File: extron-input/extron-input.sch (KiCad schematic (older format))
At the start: 16 parts, among them J1 SCART-F, J10 Conn_01x01, J11 Conn_01x01, J2 Conn_Coaxial, J3 Conn_Coaxial, J4 Conn_Coaxial, J5 Conn_Coaxial, J6 Conn_01x03_Male, J7 Conn_01x02_Male, J8 Conn_01x01, J9 Conn_01x01, SW1 SW_DPDT_x2, U1 LM1881

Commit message: Oops, scart-input -> extron-input
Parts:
- J1: footprint scart-input:SCART_F_RA -> extron-input:SCART_F_RA
- J2, J3, J4, J5: footprint scart-input:BNC_90 -> extron-input:BNC_90
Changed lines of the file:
@@
 LIBS:power
 LIBS:74xx
-LIBS:scart-input-cache
+LIBS:extron-input-cache
 EELAYER 26 0
 EELAYER END
@@
 F 0 "J2" H 8200 1550 50  0000 L CNN
 F 1 "Conn_Coaxial" H 7850 2200 50  0000 L CNN
-F 2 "scart-input:BNC_90" H 8250 2050 50  0001 C CNN
+F 2 "extron-input:BNC_90" H 8250 2050 50  0001 C CNN
 F 3 " ~" H 8250 2050 50  0001 C CNN
 	1    8250 2050
@@
 F 0 "J3" H 8200 2400 50  0000 L CNN
 F 1 "Conn_Coaxial" H 7850 3050 50  0000 L CNN
-F 2 "scart-input:BNC_90" H 8250 2900 50  0001 C CNN
+F 2 "extron-input:BNC_90" H 8250 2900 50  0001 C CNN
 F 3 " ~" H 8250 2900 50  0001 C CNN
 	1    8250 2900
@@
 F 0 "J4" H 8200 3250 50  0000 L CNN
 F 1 "Conn_Coaxial" H 7850 3900 50  0000 L CNN
-F 2 "scart-input:BNC_90" H 8250 3750 50  0001 C CNN
+F 2 "extron-input:BNC_90" H 8250 3750 50  0001 C CNN
 F 3 " ~" H 8250 3750 50  0001 C CNN
 	1    8250 3750
@@
 F 0 "J5" H 8200 4050 50  0000 L CNN
 F 1 "Conn_Coaxial" H 7850 4700 50  0000 L CNN
-F 2 "scart-input:BNC_90" H 8250 4550 50  0001 C CNN
+F 2 "extron-input:BNC_90" H 8250 4550 50  0001 C CNN
 F 3 " ~" H 8250 4550 50  0001 C CNN
 	1    8250 4550
@@
 F 0 "J1" H 3850 4520 50  0000 C CNN
 F 1 "SCART-F" H 3850 4429 50  0000 C CNN
-F 2 "scart-input:SCART_F_RA" H 3850 3150 50  0001 C CNN
+F 2 "extron-input:SCART_F_RA" H 3850 3150 50  0001 C CNN
 F 3 " ~" H 3850 3150 50  0001 C CNN
 	1    3850 3100

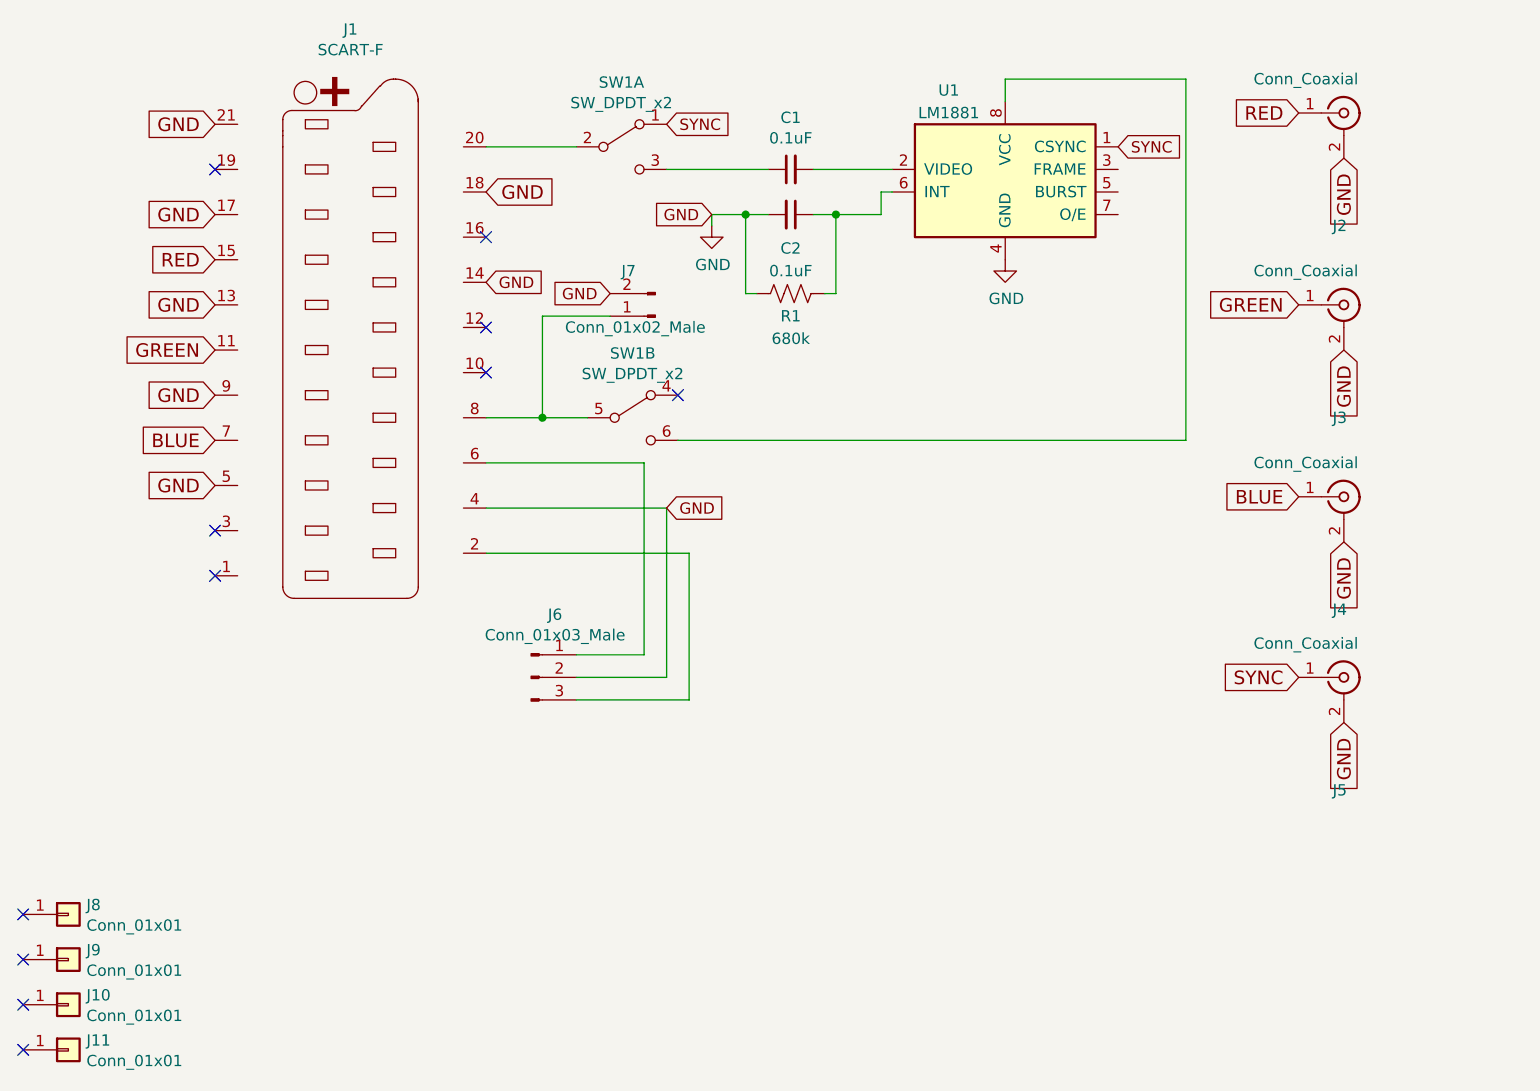
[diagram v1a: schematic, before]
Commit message: Random fixes to extron-input layout/schematic
There were some weirdnesses between the schematic and layout. I believe
these are fixed now.

I also switched the footprint to JST XH side connectors for both sense
and phoenix ports. I found that there are cables that can be purchased
for cheap for this form factor.
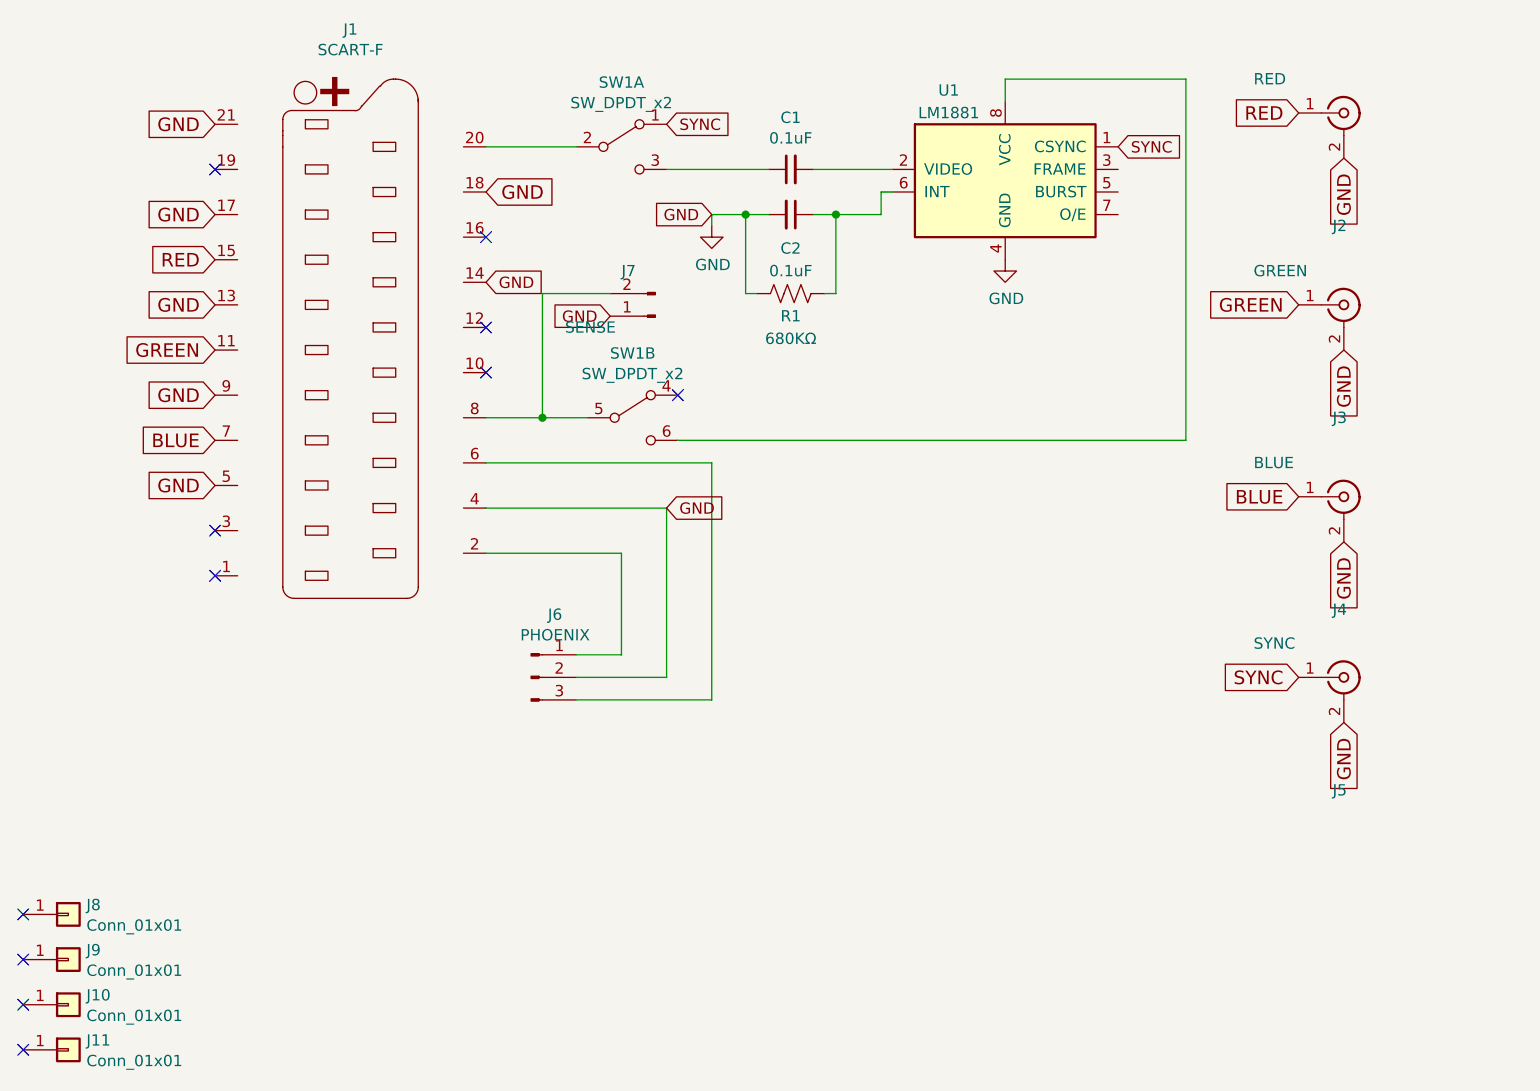
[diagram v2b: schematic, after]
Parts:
- J2: value Conn_Coaxial -> RED
- J3: value Conn_Coaxial -> GREEN
- J4: value Conn_Coaxial -> BLUE
- J5: value Conn_Coaxial -> SYNC
- J6: value Conn_01x03_Male -> PHOENIX; footprint Connector_JST:JST_EH_S03B-EH_1x03_P2.50mm_Horizontal -> Connector_JST:JST_XH_S03B-XH-A_1x03_P2.50mm_Horizontal
- J7: value Conn_01x02_Male -> SENSE; footprint Connector_JST:JST_EH_S02B-EH_1x02_P2.50mm_Horizontal -> Connector_JST:JST_XH_S02B-XH-A_1x02_P2.50mm_Horizontal
- R1: value 680k -> 680KΩ
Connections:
- net GND: now also J7.1 (Pin_1); no longer J7.2 (Pin_2)
- net at J1.2 (P2): now also J6.1 (Pin_1); no longer J6.3 (Pin_3)
- net at J1.6 (P6): now also J6.3 (Pin_3); no longer J6.1 (Pin_1)
- net at J1.8 (P8), SW1.5 (B): now also J7.2 (Pin_2); no longer J7.1 (Pin_1)
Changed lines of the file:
@@
 P 8250 2050
 F 0 "J2" H 8200 1550 50  0000 L CNN
-F 1 "Conn_Coaxial" H 7850 2200 50  0000 L CNN
+F 1 "RED" H 7850 2200 50  0000 L CNN
 F 2 "extron-input:BNC_90" H 8250 2050 50  0001 C CNN
 F 3 " ~" H 8250 2050 50  0001 C CNN
@@
 P 8250 2900
 F 0 "J3" H 8200 2400 50  0000 L CNN
-F 1 "Conn_Coaxial" H 7850 3050 50  0000 L CNN
+F 1 "GREEN" H 7850 3050 50  0000 L CNN
 F 2 "extron-input:BNC_90" H 8250 2900 50  0001 C CNN
 F 3 " ~" H 8250 2900 50  0001 C CNN
@@
 P 8250 3750
 F 0 "J4" H 8200 3250 50  0000 L CNN
-F 1 "Conn_Coaxial" H 7850 3900 50  0000 L CNN
+F 1 "BLUE" H 7850 3900 50  0000 L CNN
 F 2 "extron-input:BNC_90" H 8250 3750 50  0001 C CNN
 F 3 " ~" H 8250 3750 50  0001 C CNN
@@
 P 8250 4550
 F 0 "J5" H 8200 4050 50  0000 L CNN
-F 1 "Conn_Coaxial" H 7850 4700 50  0000 L CNN
+F 1 "SYNC" H 7850 4700 50  0000 L CNN
 F 2 "extron-input:BNC_90" H 8250 4550 50  0001 C CNN
 F 3 " ~" H 8250 4550 50  0001 C CNN
@@
 P 4650 4550
 F 0 "J6" H 4756 4828 50  0000 C CNN
-F 1 "Conn_01x03_Male" H 4756 4737 50  0000 C CNN
-F 2 "Connector_JST:JST_EH_S03B-EH_1x03_P2.50mm_Horizontal" H 4650 4550 50  0001 C CNN
+F 1 "PHOENIX" H 4756 4737 50  0000 C CNN
+F 2 "Connector_JST:JST_XH_S03B-XH-A_1x03_P2.50mm_Horizontal" H 4650 4550 50  0001 C CNN
 F 3 "~" H 4650 4550 50  0001 C CNN
 	1    4650 4550
@@
 P 5200 2950
 F 0 "J7" H 5350 2750 50  0000 R CNN
-F 1 "Conn_01x02_Male" H 5600 3000 50  0000 R CNN
-F 2 "Connector_JST:JST_EH_S02B-EH_1x02_P2.50mm_Horizontal" H 5200 2950 50  0001 C CNN
+F 1 "SENSE" H 5600 3000 50  0000 R CNN
+F 2 "Connector_JST:JST_XH_S02B-XH-A_1x02_P2.50mm_Horizontal" H 5200 2950 50  0001 C CNN
 F 3 "~" H 5200 2950 50  0001 C CNN
 	1    5200 2950
@@
 P 5800 2850
 F 0 "R1" V 5700 2850 50  0000 C CNN
-F 1 "680k" V 5600 2850 50  0000 C CNN
+F 1 "680KΩ" V 5600 2850 50  0000 C CNN
 F 2 "Resistor_THT:R_Axial_DIN0204_L3.6mm_D1.6mm_P1.90mm_Vertical" V 5840 2840 50  0001 C CNN
 F 3 "~" H 5800 2850 50  0001 C CNN
@@
 	5300 3500 7550 3500
 Wire Wire Line
-	4450 3600 5150 3600
-Wire Wire Line
-	5150 3600 5150 4450
-Wire Wire Line
-	5150 4450 4850 4450
-Wire Wire Line
 	4450 3800 5250 3800
 Wire Wire Line
@@
 Wire Wire Line
 	5250 3800 5250 4550
-Wire Wire Line
-	4450 4000 5350 4000
-Wire Wire Line
-	5350 4000 5350 4650
-Wire Wire Line
-	5350 4650 4850 4650
 Text GLabel 4450 2800 2    50   Input ~ 0
 GND
-Wire Wire Line
-	5000 2950 4700 2950
-Wire Wire Line
-	4700 2950 4700 3400
 Connection ~ 4700 3400
 Wire Wire Line
 	4700 3400 4900 3400
-Text GLabel 5000 2850 0    50   Input ~ 0
+Text GLabel 5000 2950 0    50   Input ~ 0
 GND
 Wire Wire Line
@@
 	1    0    0    -1
 $EndComp
+Wire Wire Line
+	4450 4000 5050 4000
+Wire Wire Line
+	5050 4000 5050 4450
+Wire Wire Line
+	5050 4450 4850 4450
+Wire Wire Line
+	5450 3600 5450 4650
+Wire Wire Line
+	4450 3600 5450 3600
+Wire Wire Line
+	4850 4650 5450 4650
+Wire Wire Line
+	4700 2850 5000 2850
+Wire Wire Line
+	4700 2850 4700 3400
 $EndSCHEMATC
